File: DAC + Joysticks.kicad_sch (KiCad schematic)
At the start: 127 parts, among them J10 L Phono, J11 R Phono, J8 JOY0, J9 JOY1, U23 74HC374, U24 74HC374, U25 74LS244, U26 74LS244, U27 74LS373, U28 74LS244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

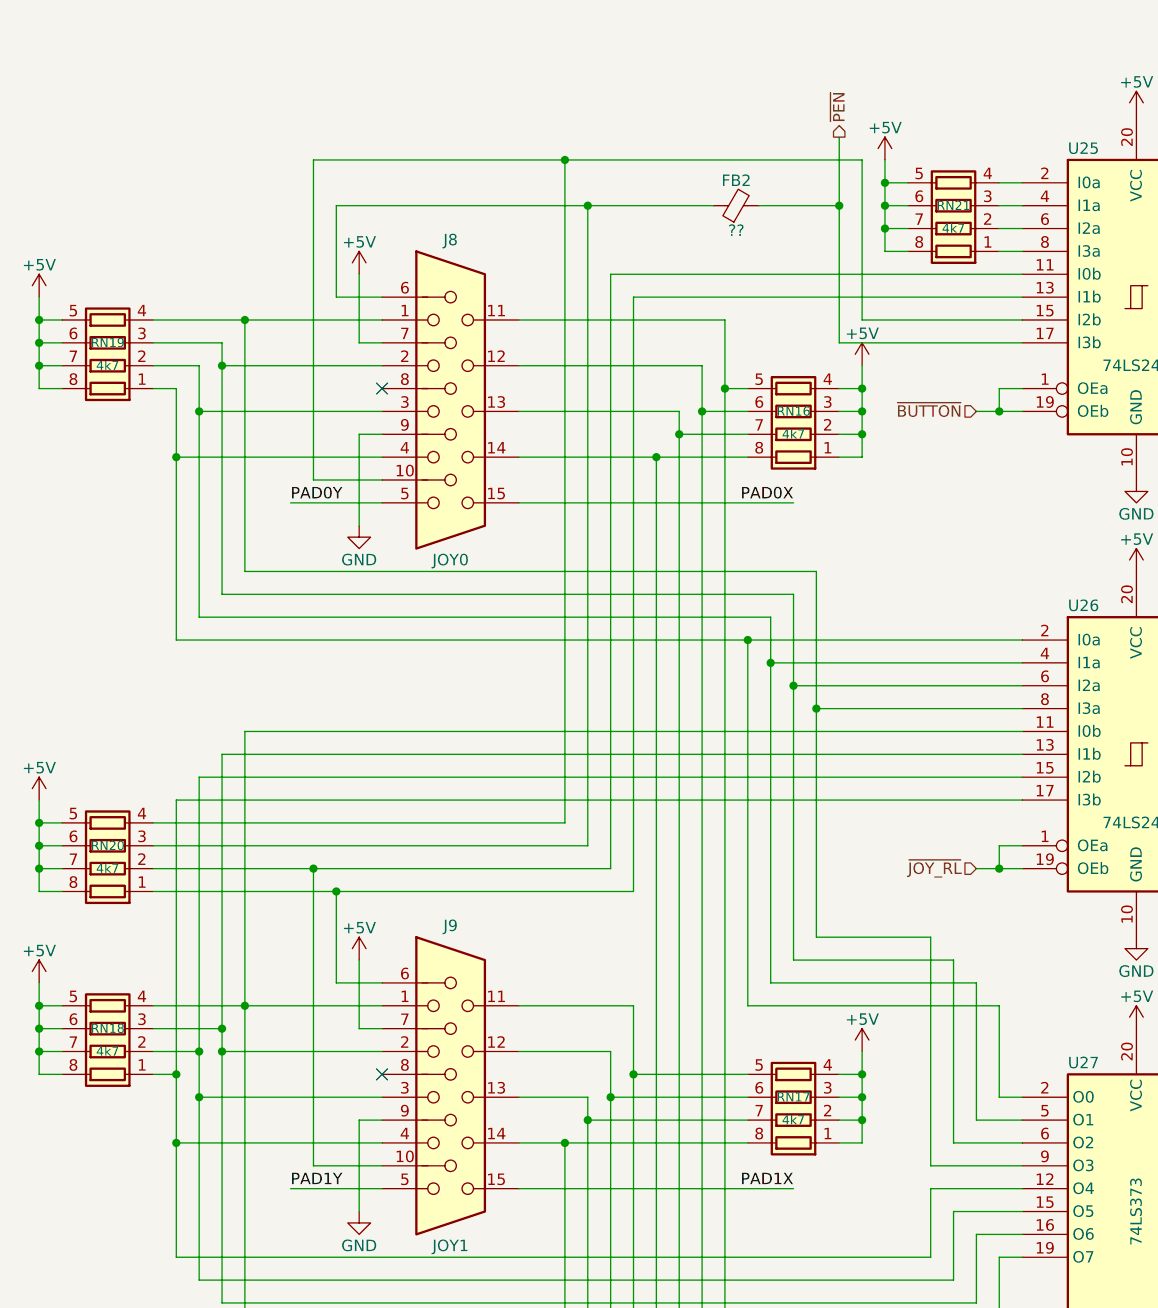
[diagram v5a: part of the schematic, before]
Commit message: motherboard: Fixed a pile of resistor network issues, and concluded initial routing of the CPU and audio amp passives
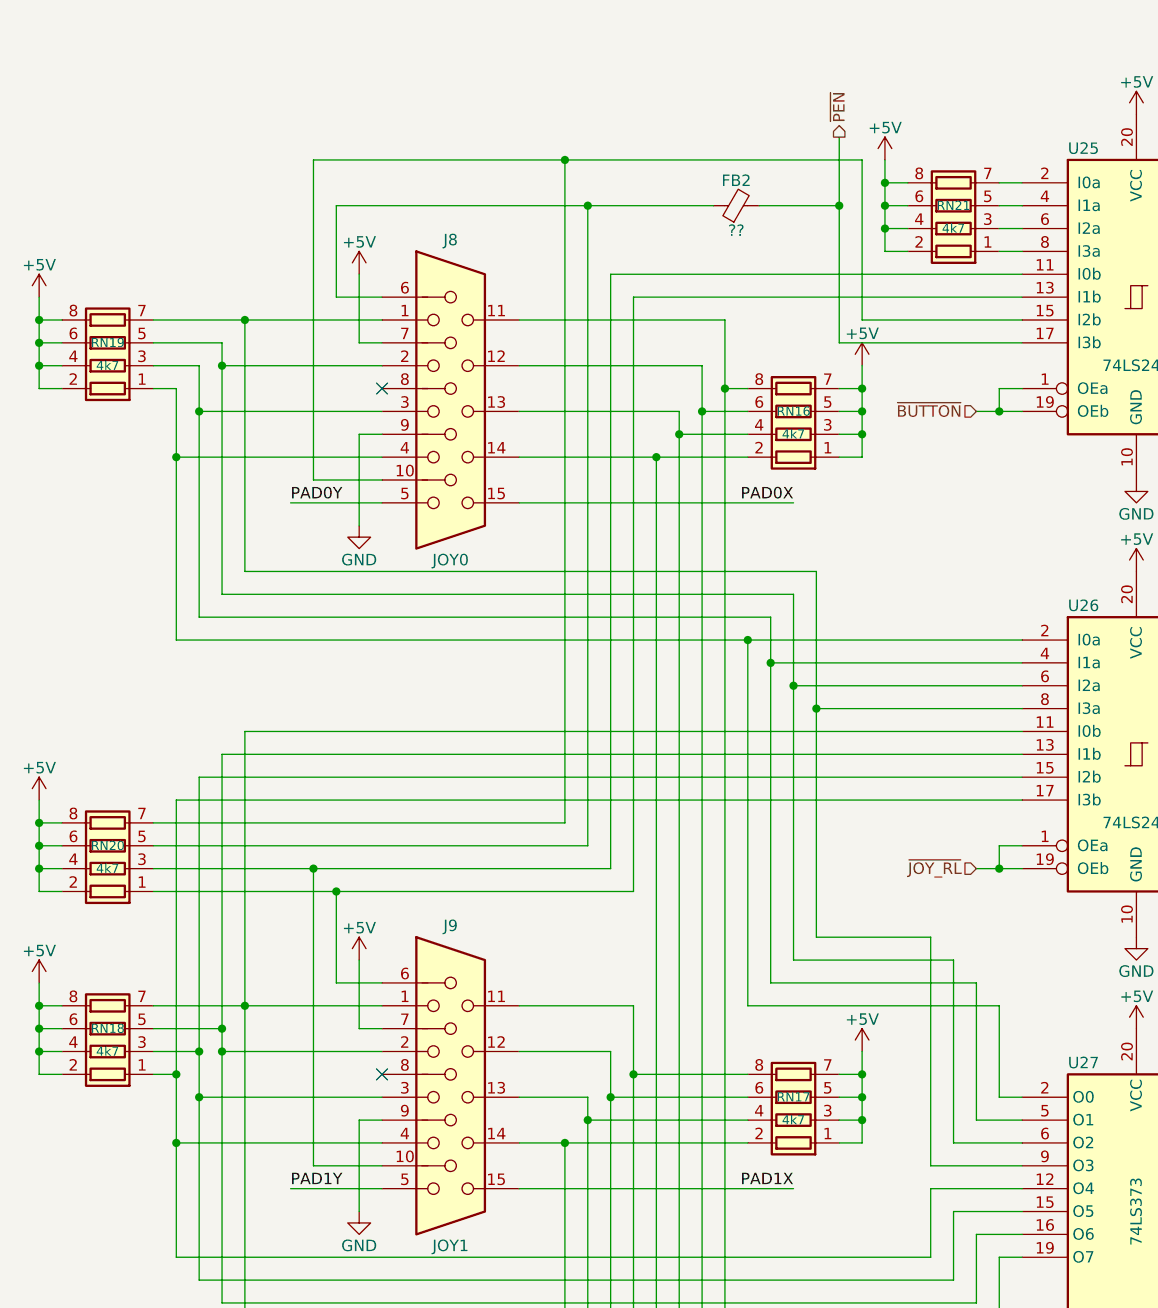
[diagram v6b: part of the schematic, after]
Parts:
- RN16, RN17, RN18, RN19, RN20, RN21: symbol Device:R_Pack04 -> dragonmux:R_Pack04_OddEven
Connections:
- net +5V: now also RN16.5 (R4.2), RN16.7 (R2.2), RN17.5 (R4.2), RN17.7 (R2.2), RN18.2 (R2.1), RN18.4 (R4.1), RN19.2 (R2.1), RN19.4 (R4.1), RN20.2 (R2.1), RN20.4 (R4.1), RN21.2 (R2.1), RN21.4 (R4.1); no longer RN16.2 (R2.1), RN16.4 (R4.1), RN17.2 (R2.1), RN17.4 (R4.1), RN18.5 (R4.2), RN18.7 (R2.2), RN19.5 (R4.2), RN19.7 (R2.2), RN20.5 (R4.2), RN20.7 (R2.2), RN21.5 (R4.2), RN21.7 (R2.2)
- net at U25.6 (I2a): now also RN21.3 (R3.1); no longer RN21.2 (R2.1)
- net at U25.4 (I1a): now also RN21.5 (R4.2); no longer RN21.3 (R3.1)
- net at U25.2 (I0a): now also RN21.7 (R2.2); no longer RN21.4 (R4.1)
- net at J9.3, U26.15 (I2b), U27.15 (O5): now also RN18.3 (R3.1); no longer RN18.2 (R2.1)
- net at J9.2, U26.13 (I1b), U27.16 (O6): now also RN18.5 (R4.2); no longer RN18.3 (R3.1)
- net at J9.1, U26.11 (I0b), U27.19 (O7): now also RN18.7 (R2.2); no longer RN18.4 (R4.1)
- net at FB2.1, J8.6: now also RN20.5 (R4.2); no longer RN20.3 (R3.1)
- net at J9.14, U28.11 (I0b): now also RN17.2 (R2.1); no longer RN17.8 (R1.2)
- net at J9.13, U28.13 (I1b): now also RN17.4 (R4.1); no longer RN17.7 (R2.2)
- net at J9.11, U28.17 (I3b): now also RN17.8 (R1.2); no longer RN17.5 (R4.2)
- net at J8.14, U28.2 (I0a): now also RN16.2 (R2.1); no longer RN16.8 (R1.2)
- net at J8.13, U28.4 (I1a): now also RN16.4 (R4.1); no longer RN16.7 (R2.2)
- net at J8.11, U28.8 (I3a): now also RN16.8 (R1.2); no longer RN16.5 (R4.2)
- net at J8.1, U26.8 (I3a), U27.9 (O3): now also RN19.7 (R2.2); no longer RN19.4 (R4.1)
- net at J8.10, U25.15 (I2b): now also RN20.7 (R2.2); no longer RN20.4 (R4.1)
- net at J8.2, U26.6 (I2a), U27.6 (O2): now also RN19.5 (R4.2); no longer RN19.3 (R3.1)
- net at J8.3, U26.4 (I1a), U27.5 (O1): now also RN19.3 (R3.1); no longer RN19.2 (R2.1)
- net at J9.10, U25.11 (I0b): now also RN20.3 (R3.1); no longer RN20.2 (R2.1)
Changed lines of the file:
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@@
 	)
 	(symbol
-		(lib_id "Device:R_Pack04")
+		(lib_id "dragonmux:R_Pack04_OddEven")
 		(at 119.38 40.64 90)
 		(unit 1)
@@
 		)
 		(property "Description" "4 resistor network, parallel topology"
-			(at 119.38 40.64 0)
+			(at 132.08 41.91 0)
 			(effects
 				(font
@@
 	)
 	(symbol
-		(lib_id "Device:R_Pack04")
+		(lib_id "dragonmux:R_Pack04_OddEven")
 		(at 25.4 132.08 90)
 		(unit 1)
@@
 		)
 		(property "Description" "4 resistor network, parallel topology"
-			(at 25.4 132.08 0)
+			(at 38.1 133.35 0)
 			(effects
 				(font
@@
 	)
 	(symbol
-		(lib_id "Device:R_Pack04")
+		(lib_id "dragonmux:R_Pack04_OddEven")
 		(at 101.6 63.5 90)
 		(unit 1)
@@
 		)
 		(property "Description" "4 resistor network, parallel topology"
-			(at 101.6 63.5 0)
+			(at 114.3 64.77 0)
 			(effects
 				(font
@@
 	)
 	(symbol
-		(lib_id "Device:R_Pack04")
+		(lib_id "dragonmux:R_Pack04_OddEven")
 		(at 25.4 111.76 90)
 		(unit 1)
@@
 		)
 		(property "Description" "4 resistor network, parallel topology"
-			(at 25.4 111.76 0)
+			(at 38.1 113.03 0)
 			(effects
 				(font
@@
 	)
 	(symbol
-		(lib_id "Device:R_Pack04")
+		(lib_id "dragonmux:R_Pack04_OddEven")
 		(at 25.4 55.88 90)
 		(unit 1)
@@
 		)
 		(property "Description" "4 resistor network, parallel topology"
-			(at 25.4 55.88 0)
+			(at 38.1 57.15 0)
 			(effects
 				(font
@@
 	)
 	(symbol
-		(lib_id "Device:R_Pack04")
+		(lib_id "dragonmux:R_Pack04_OddEven")
 		(at 101.6 139.7 90)
 		(unit 1)
@@
 		)
 		(property "Description" "4 resistor network, parallel topology"
-			(at 101.6 139.7 0)
+			(at 114.3 140.97 0)
 			(effects
 				(font

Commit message: motherboard: Added packaging and ordering information for many of the 7400 logic parts and the DACs
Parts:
- U23, U24: footprint (none) -> Package_SO:SO-20_12.8x7.5mm_P1.27mm; MFR (none) -> Nexperia; MPN (none) -> 74HC374D,653; OC_FARNELL (none) -> 1085342
- U25, U26, U28: value 74LS244 -> 74HC244; footprint (none) -> Package_SO:SO-20_12.8x7.5mm_P1.27mm; MFR (none) -> Nexperia; MPN (none) -> 74HC244D,653; OC_FARNELL (none) -> 1201322
- U27: value 74LS373 -> 74HC373; footprint (none) -> Package_SO:SO-20_12.8x7.5mm_P1.27mm; MFR (none) -> Nexperia; MPN (none) -> 74HC373D,653; OC_FARNELL (none) -> 1085341
- U29, U31: footprint (none) -> Package_SO:SO-16_3.9x9.9mm_P1.27mm
- U34: footprint Package_DIP:DIP-28_W15.24mm_Socket -> rhais_package-dip:DIP-28_W15.24mm_Socket
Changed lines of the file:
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@@
 			)
 		)
-		(property "Footprint" "Package_DIP:DIP-28_W15.24mm_Socket"
+		(property "Footprint" "rhais_package-dip:DIP-28_W15.24mm_Socket"
 			(at 292.1 203.2 0)
 			(effects
@@
 			)
 		)
-		(property "Value" "74LS244"
+		(property "Value" "74HC244"
 			(at 139.7 210.82 0)
 			(effects
@@
 			)
 		)
-		(property "Footprint" ""
+		(property "Footprint" "Package_SO:SO-20_12.8x7.5mm_P1.27mm"
 			(at 139.7 203.2 0)
 			(effects
@@
 			)
 		)
-		(property "Datasheet" "http://www.ti.com/lit/ds/symlink/sn74ls244.pdf"
+		(property "Datasheet" "https://assets.nexperia.com/documents/data-sheet/74AHC_AHCT244.pdf"
 			(at 139.7 203.2 0)
 			(effects
@@
 			)
 		)
+		(property "MFR" "Nexperia"
+			(at 139.7 203.2 0)
+			(effects
+				(font
+					(size 1.27 1.27)
+				)
+				(hide yes)
+			)
+		)
+		(property "MPN" "74HC244D,653"
+			(at 139.7 203.2 0)
+			(effects
+				(font
+					(size 1.27 1.27)
+				)
+				(hide yes)
+			)
+		)
+		(property "OC_FARNELL" "1201322"
+			(at 139.7 203.2 0)
+			(effects
+				(font
+					(size 1.27 1.27)
+				)
+				(hide yes)
+			)
+		)
 		(pin "6"
 		)
@@
 			)
 		)
-		(property "Footprint" ""
+		(property "Footprint" "Package_SO:SO-16_3.9x9.9mm_P1.27mm"
 			(at 256.54 123.19 0)
 			(effects
@@
 			)
 		)
-		(property "Value" "74LS244"
+		(property "Value" "74HC244"
 			(at 139.7 58.42 0)
 			(effects
@@
 			)
 		)
-		(property "Footprint" ""
+		(property "Footprint" "Package_SO:SO-20_12.8x7.5mm_P1.27mm"
 			(at 139.7 50.8 0)
 			(effects
@@
 			)
 		)
-		(property "Datasheet" "http://www.ti.com/lit/ds/symlink/sn74ls244.pdf"
+		(property "Datasheet" "https://assets.nexperia.com/documents/data-sheet/74AHC_AHCT244.pdf"
 			(at 139.7 50.8 0)
 			(effects
@@
 			)
 		)
+		(property "MFR" "Nexperia"
+			(at 139.7 50.8 0)
+			(effects
+				(font
+					(size 1.27 1.27)
+				)
+				(hide yes)
+			)
+		)
+		(property "MPN" "74HC244D,653"
+			(at 139.7 50.8 0)
+			(effects
+				(font
+					(size 1.27 1.27)
+				)
+				(hide yes)
+			)
+		)
+		(property "OC_FARNELL" "1201322"
+			(at 139.7 50.8 0)
+			(effects
+				(font
+					(size 1.27 1.27)
+				)
+				(hide yes)
+			)
+		)
 		(pin "6"
 		)
@@
 			)
 		)
-		(property "Value" "74LS373"
+		(property "Value" "74HC373"
 			(at 139.7 152.4 90)
 			(effects
@@
 			)
 		)
-		(property "Footprint" ""
+		(property "Footprint" "Package_SO:SO-20_12.8x7.5mm_P1.27mm"
 			(at 139.7 152.4 0)
 			(effects
@@
 			)
 		)
-		(property "Datasheet" "http://www.ti.com/lit/gpn/sn74LS373"
+		(property "Datasheet" "https://assets.nexperia.com/documents/data-sheet/74HC_HCT373.pdf"
 			(at 139.7 152.4 0)
 			(effects
@@
 			)
 		)
+		(property "MFR" "Nexperia"
+			(at 139.7 152.4 0)
+			(effects
+				(font
+					(size 1.27 1.27)
+				)
+				(hide yes)
+			)
+		)
+		(property "MPN" "74HC373D,653"
+			(at 139.7 152.4 0)
+			(effects
+				(font
+					(size 1.27 1.27)
+				)
+				(hide yes)
+			)
+		)
+		(property "OC_FARNELL" "1085341"
+			(at 139.7 152.4 0)
+			(effects
+				(font
+					(size 1.27 1.27)
+				)
+				(hide yes)
+			)
+		)
 		(pin "8"
 		)
@@
 			)
 		)
-		(property "Footprint" ""
+		(property "Footprint" "Package_SO:SO-16_3.9x9.9mm_P1.27mm"
 			(at 256.54 59.69 0)
 			(effects
@@
 			)
 		)
-		(property "Footprint" ""
+		(property "Footprint" "Package_SO:SO-20_12.8x7.5mm_P1.27mm"
 			(at 215.9 127 0)
 			(effects
@@
 			)
 		)
-		(property "Datasheet" "https://www.ti.com/lit/ds/symlink/cd74hct374.pdf"
+		(property "Datasheet" "https://assets.nexperia.com/documents/data-sheet/74HC_HCT374.pdf"
 			(at 215.9 127 0)
 			(effects
@@
 			)
 		)
+		(property "MFR" "Nexperia"
+			(at 215.9 127 0)
+			(effects
+				(font
+					(size 1.27 1.27)
+				)
+				(hide yes)
+			)
+		)
+		(property "MPN" "74HC374D,653"
+			(at 215.9 127 0)
+			(effects
+				(font
+					(size 1.27 1.27)
+				)
+				(hide yes)
+			)
+		)
+		(property "OC_FARNELL" "1085342"
+			(at 215.9 127 0)
+			(effects
+				(font
+					(size 1.27 1.27)
+				)
+				(hide yes)
+			)
+		)
 		(pin "11"
 		)
@@
 			)
 		)
-		(property "Value" "74LS244"
+		(property "Value" "74HC244"
 			(at 139.7 109.22 0)
 			(effects
@@
 			)
 		)
-		(property "Footprint" ""
+		(property "Footprint" "Package_SO:SO-20_12.8x7.5mm_P1.27mm"
 			(at 139.7 101.6 0)
 			(effects
@@
 			)
 		)
-		(property "Datasheet" "http://www.ti.com/lit/ds/symlink/sn74ls244.pdf"
+		(property "Datasheet" "https://assets.nexperia.com/documents/data-sheet/74AHC_AHCT244.pdf"
 			(at 139.7 101.6 0)
 			(effects
@@
 			)
 		)
+		(property "MFR" "Nexperia"
+			(at 139.7 101.6 0)
+			(effects
+				(font
+					(size 1.27 1.27)
+				)
+				(hide yes)
+			)
+		)
+		(property "MPN" "74HC244D,653"
+			(at 139.7 101.6 0)
+			(effects
+				(font
+					(size 1.27 1.27)
+				)
+				(hide yes)
+			)
+		)
+		(property "OC_FARNELL" "1201322"
+			(at 139.7 101.6 0)
+			(effects
+				(font
+					(size 1.27 1.27)
+				)
+				(hide yes)
+			)
+		)
 		(pin "6"
 		)
@@
 			)
 		)
-		(property "Footprint" ""
+		(property "Footprint" "Package_SO:SO-20_12.8x7.5mm_P1.27mm"
 			(at 215.9 63.5 0)
 			(effects
@@
 			)
 		)
-		(property "Datasheet" "https://www.ti.com/lit/ds/symlink/cd74hct374.pdf"
+		(property "Datasheet" "https://assets.nexperia.com/documents/data-sheet/74HC_HCT374.pdf"
 			(at 215.9 63.5 0)
 			(effects
@@
 			(at 215.9 63.5 0)
 			(effects
+				(font
+					(size 1.27 1.27)
+				)
+				(hide yes)
+			)
+		)
+		(property "MFR" "Nexperia"
+			(at 215.9 63.5 0)
+			(effects
+				(font
+					(size 1.27 1.27)
+				)
+				(hide yes)
+			)
+		)
+		(property "MPN" "74HC374D,653"
+			(at 215.9 63.5 0)
+			(effects
+				(font
+					(size 1.27 1.27)
+				)
+				(hide yes)
+			)
+		)
+		(property "OC_FARNELL" "1085342"
+			(at 215.9 63.5 0)
+			(effects

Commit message: motherboard: Routed out the bulk of the DAC section and feed latches
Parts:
- J8, J9: footprint (none) -> Connector_Dsub:DSUB-15_Socket_Horizontal_P2.77x2.54mm_EdgePinOffset9.40mm
- U23, U24, U25, U26, U27, U28: footprint Package_SO:SO-20_12.8x7.5mm_P1.27mm -> rhais_package-smd:SO-20_12.8x7.5mm_P1.27mm
- U29, U31: footprint Package_SO:SO-16_3.9x9.9mm_P1.27mm -> rhais_package-smd:SO-16_3.9x9.9mm_P1.27mm; MFR (none) -> TI; MPN (none) -> DAC0802; URL_TI (none) -> https://www.ti.com/product/DAC0802/part-details/DAC0802LCMX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
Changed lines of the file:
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@@
 			)
 		)
-		(property "Footprint" "Package_SO:SO-20_12.8x7.5mm_P1.27mm"
+		(property "Footprint" "rhais_package-smd:SO-20_12.8x7.5mm_P1.27mm"
 			(at 139.7 203.2 0)
 			(effects
@@
 			)
 		)
-		(property "Footprint" "Package_SO:SO-16_3.9x9.9mm_P1.27mm"
+		(property "Footprint" "rhais_package-smd:SO-16_3.9x9.9mm_P1.27mm"
 			(at 256.54 123.19 0)
 			(effects
@@
 			)
 		)
+		(property "MFR" "TI"
+			(at 256.54 123.19 0)
+			(effects
+				(font
+					(size 1.27 1.27)
+				)
+				(hide yes)
+			)
+		)
+		(property "MPN" "DAC0802"
+			(at 256.54 123.19 0)
+			(effects
+				(font
+					(size 1.27 1.27)
+				)
+				(hide yes)
+			)
+		)
+		(property "OC_FARNELL" ""
+			(at 256.54 123.19 0)
+			(effects
+				(font
+					(size 1.27 1.27)
+				)
+				(hide yes)
+			)
+		)
+		(property "URL_TI" "https://www.ti.com/product/DAC0802/part-details/DAC0802LCMX/NOPB"
+			(at 256.54 123.19 0)
+			(effects
+				(font
+					(size 1.27 1.27)
+				)
+				(hide yes)
+			)
+		)
 		(pin "8"
 		)
@@
 			)
 		)
-		(property "Footprint" ""
+		(property "Footprint" "Connector_Dsub:DSUB-15_Socket_Horizontal_P2.77x2.54mm_EdgePinOffset9.40mm"
 			(at 39.37 53.34 0)
 			(effects
@@
 			)
 		)
-		(property "Footprint" "Package_SO:SO-20_12.8x7.5mm_P1.27mm"
+		(property "Footprint" "rhais_package-smd:SO-20_12.8x7.5mm_P1.27mm"
 			(at 139.7 50.8 0)
 			(effects
@@
 			)
 		)
-		(property "Footprint" "Package_SO:SO-20_12.8x7.5mm_P1.27mm"
+		(property "Footprint" "rhais_package-smd:SO-20_12.8x7.5mm_P1.27mm"
 			(at 139.7 152.4 0)
 			(effects
@@
 			)
 		)
-		(property "Footprint" ""
+		(property "Footprint" "Connector_Dsub:DSUB-15_Socket_Horizontal_P2.77x2.54mm_EdgePinOffset9.40mm"
 			(at 39.37 129.54 0)
 			(effects
@@
 			)
 		)
-		(property "Footprint" "Package_SO:SO-16_3.9x9.9mm_P1.27mm"
+		(property "Footprint" "rhais_package-smd:SO-16_3.9x9.9mm_P1.27mm"
 			(at 256.54 59.69 0)
 			(effects
@@
 			)
 		)
+		(property "MFR" "TI"
+			(at 256.54 59.69 0)
+			(effects
+				(font
+					(size 1.27 1.27)
+				)
+				(hide yes)
+			)
+		)
+		(property "MPN" "DAC0802"
+			(at 256.54 59.69 0)
+			(effects
+				(font
+					(size 1.27 1.27)
+				)
+				(hide yes)
+			)
+		)
+		(property "URL_TI" "https://www.ti.com/product/DAC0802/part-details/DAC0802LCMX/NOPB"
+			(at 256.54 59.69 0)
+			(effects
+				(font
+					(size 1.27 1.27)
+				)
+				(hide yes)
+			)
+		)
+		(property "OC_FARNELL" ""
+			(at 256.54 59.69 0)
+			(effects
+				(font
+					(size 1.27 1.27)
+				)
+				(hide yes)
+			)
+		)
 		(pin "8"
 		)
@@
 			)
 		)
-		(property "Footprint" "Package_SO:SO-20_12.8x7.5mm_P1.27mm"
+		(property "Footprint" "rhais_package-smd:SO-20_12.8x7.5mm_P1.27mm"
 			(at 215.9 127 0)
 			(effects
@@
 			)
 		)
-		(property "Footprint" "Package_SO:SO-20_12.8x7.5mm_P1.27mm"
+		(property "Footprint" "rhais_package-smd:SO-20_12.8x7.5mm_P1.27mm"
 			(at 139.7 101.6 0)
 			(effects
@@
 			)
 		)
-		(property "Footprint" "Package_SO:SO-20_12.8x7.5mm_P1.27mm"
+		(property "Footprint" "rhais_package-smd:SO-20_12.8x7.5mm_P1.27mm"
 			(at 215.9 63.5 0)
 			(effects
